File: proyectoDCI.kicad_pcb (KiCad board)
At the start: 2 copper layers, 45 x 20 mm, 27 parts, among them P1 CONN_02X04, P2 CONN_01X01, P3 GSG-RF-CONN, P4 GSG-RF-CONN, U1 AD5933, U2 ADG849, U3 AD8606, U4 ASFLMB-16.000MHZ-LY-T, U5 ADP150

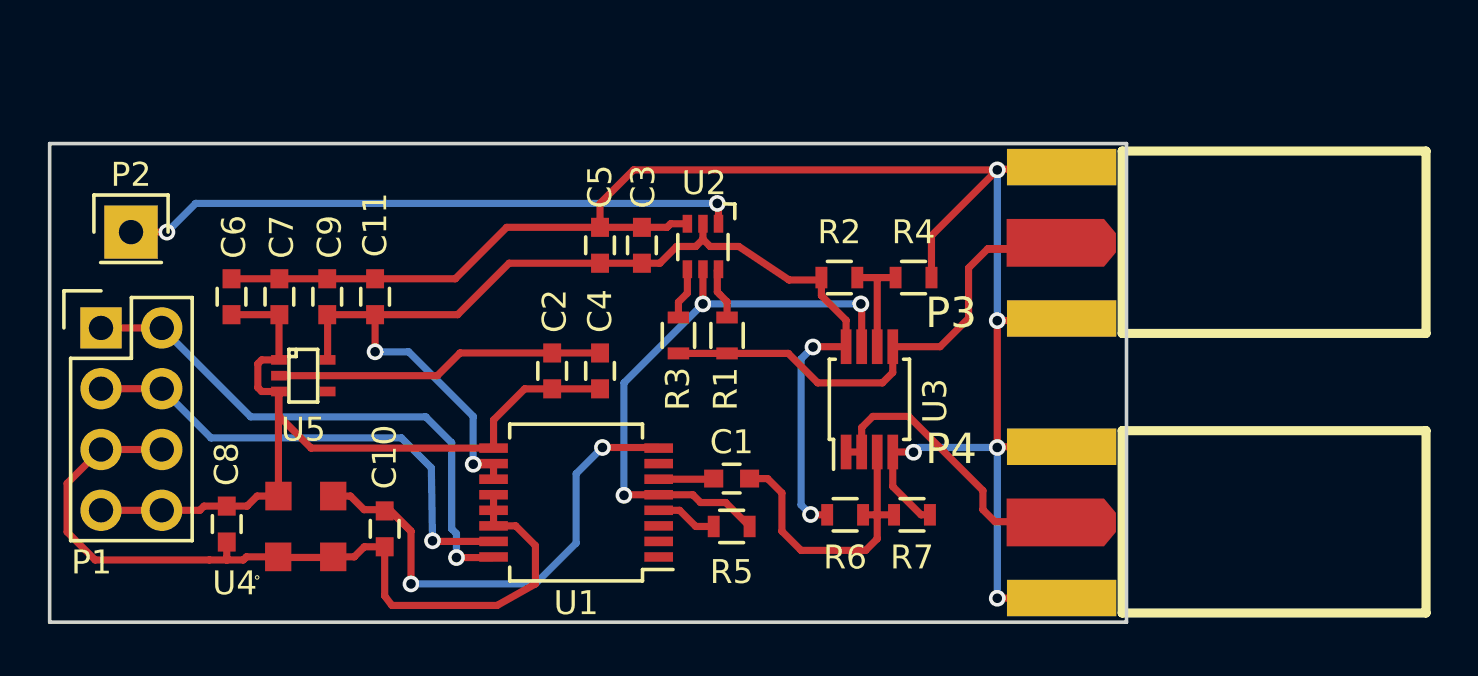
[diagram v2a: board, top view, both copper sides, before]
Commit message: Se modifico el rotulo y se agregaron aclaraciones del proceso de fabricacion
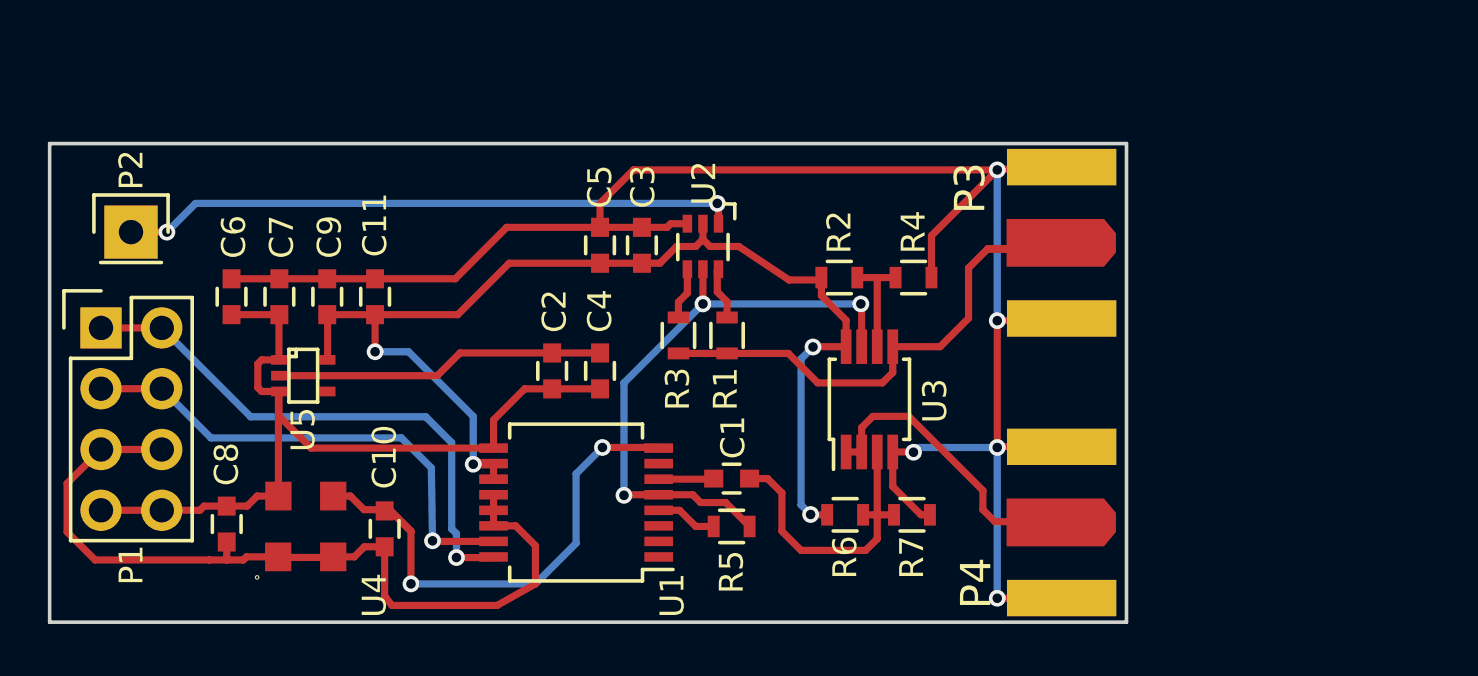
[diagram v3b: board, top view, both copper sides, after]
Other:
- board text added: "* Clearance -> 0,15 mm * Ancho de pista -> 0,15 mm * Diámetro vía -> 0,70 mm * Agujero vía -> 0,40 mm (Perfil: Mayer 6 mils ver proyectoDCI/doc/Fab)"
- board text added: "Acabado: HASL Espesor cobre: 1oz"
- board text added: "Espesor: 1,6 mm"
- board text added: "N° Capas = 2"
- board text added: "Reglas de fabricación"
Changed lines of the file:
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@@
     (area 149.924999 100.424999 195.075001 120.575001)
     (thickness 1.6)
-    (drawings 44)
+    (drawings 73)
     (tracks 241)
     (zones 0)
@@
   )
   (page A4)
+  (title_block
+    (title "PMOD Medidor de impedancia")
+    (date 2016-12-10)
+    (rev "Rev A")
+    (company CESE)
+    (comment 1 "Autor: LAROSA, F.")
+    (comment 2 "Revisor: GIGLIOTTI, E.")
+  )
   (layers
-    (0 F.Cu signal)
+    (0 F.Cu signal hide)
     (31 B.Cu signal hide)
     (32 B.Adhes user)
@@
   (module SMA_EDGE:SMA_EDGE (layer F.Cu)
     (at 201.168 115.062)
-    (fp_text reference P4 (at -13.5 -1.8) (layer F.SilkS)
+    (fp_text reference P4 (at -12.446 3.81 90) (layer F.SilkS)
       (effects (font (thickness 0.3048)))
     )
@@
       (effects (font (thickness 0.3048)))
     )
-    (fp_line (start -6.35 -2.5654) (end -6.35 5.0546) (layer F.SilkS) (width 0.381))
-    (fp_line (start -6.35 5.0546) (end 6.35 5.0546) (layer F.SilkS) (width 0.381))
-    (fp_line (start 6.35 5.0546) (end 6.35 -2.5654) (layer F.SilkS) (width 0.381))
-    (fp_line (start 6.35 -2.5654) (end -6.35 -2.5654) (layer F.SilkS) (width 0.381))
     (pad 0 connect rect (at -8.8773 -1.89484) (size 4.572 1.524) (layers *.Cu F.Mask)
       (net 2 GND))
@@
     (pad 1 connect rect (at -9.144 1.27) (size 4.07162 1.99898) (layers F.Cu F.Mask)
       (net 14 /Senal/COUT))
-    (model SMA_EDGE.wrl
+    (model /home/fsl/Documentos/ESE/Kicad/Proyecto/proyectoDCI/proyecto.3dshapes/SMAEdge.wrl
       (at (xyz -0.205 -0.05 -0.12))
-      (scale (xyz 1.3 1.3 1.3))
+      (scale (xyz 1 1 1))
       (rotate (xyz 270 0 180))
     )
@@
   (module SMA_EDGE:SMA_EDGE (layer F.Cu)
     (at 201.168 103.378)
-    (fp_text reference P3 (at -13.5 4.2) (layer F.SilkS)
+    (fp_text reference P3 (at -12.7 -1.016 90) (layer F.SilkS)
       (effects (font (thickness 0.3048)))
     )
@@
       (effects (font (thickness 0.3048)))
     )
-    (fp_line (start -6.35 -2.5654) (end -6.35 5.0546) (layer F.SilkS) (width 0.381))
-    (fp_line (start -6.35 5.0546) (end 6.35 5.0546) (layer F.SilkS) (width 0.381))
-    (fp_line (start 6.35 5.0546) (end 6.35 -2.5654) (layer F.SilkS) (width 0.381))
-    (fp_line (start 6.35 -2.5654) (end -6.35 -2.5654) (layer F.SilkS) (width 0.381))
     (pad 0 connect rect (at -8.8773 -1.89484) (size 4.572 1.524) (layers *.Cu F.Mask)
       (net 2 GND))
@@
     (pad 1 connect rect (at -9.144 1.27) (size 4.07162 1.99898) (layers F.Cu F.Mask)
       (net 15 /Senal/CIN))
-    (model SMA_EDGE.wrl
-      (at (xyz -0.205 -0.05 -0.12))
-      (scale (xyz 1.3 1.3 1.3))
-      (rotate (xyz 270 0 180))
+    (model /home/fsl/Documentos/ESE/Kicad/Proyecto/proyectoDCI/proyecto.3dshapes/SMAEdge.wrl
+      (at (xyz 0 0 0))
+      (scale (xyz 1 1 1))
+      (rotate (xyz 0 0 0))
     )
   )
   (module propios:TCXO (layer F.Cu)
     (at 160.7 116.5)
-    (fp_text reference U4 (at -2.966 2.372) (layer F.SilkS)
+    (fp_text reference U4 (at 2.876 2.88 90) (layer F.SilkS)
       (effects (font (size 1 1) (thickness 0.15)))
     )
@@
     (pad 3 smd rect (at 1.15 -1.27) (size 1.1 1.2) (layers F.Cu F.Paste F.Mask)
       (net 9 /Otros/MCLK))
+    (model Oscillators.3dshapes/TCXO_G158.wrl
+      (at (xyz 0 0 0))
+      (scale (xyz 0.15 0.3 0.3))
+      (rotate (xyz 0 0 90))
+    )
   )
   (module Capacitors_SMD:C_0603 (layer F.Cu)
@@
     (tags "capacitor 0603")
     (attr smd)
-    (fp_text reference C1 (at 0 1.524 180) (layer F.SilkS)
+    (fp_text reference C1 (at -0.062 1.724 270) (layer F.SilkS)
       (effects (font (size 1 1) (thickness 0.15)))
     )
@@
     (tags "resistor 0603")
     (attr smd)
-    (fp_text reference R2 (at 0 -1.9) (layer F.SilkS)
+    (fp_text reference R2 (at 0 -1.9 90) (layer F.SilkS)
       (effects (font (size 1 1) (thickness 0.15)))
     )
@@
     (tags "resistor 0603")
     (attr smd)
-    (fp_text reference R4 (at 0 -1.9) (layer F.SilkS)
+    (fp_text reference R4 (at 0 -1.9 90) (layer F.SilkS)
       (effects (font (size 1 1) (thickness 0.15)))
     )
@@
     (tags "resistor 0603")
     (attr smd)
-    (fp_text reference R5 (at 0 -1.9 180) (layer F.SilkS)
+    (fp_text reference R5 (at 0 -1.9 270) (layer F.SilkS)
       (effects (font (size 1 1) (thickness 0.15)))
     )
@@
     (tags "resistor 0603")
     (attr smd)
-    (fp_text reference R6 (at 0 1.778) (layer F.SilkS)
+    (fp_text reference R6 (at 0 1.778 90) (layer F.SilkS)
       (effects (font (size 1 1) (thickness 0.15)))
     )
@@
     (tags "resistor 0603")
     (attr smd)
-    (fp_text reference R7 (at 0 1.778) (layer F.SilkS)
+    (fp_text reference R7 (at 0 1.778 90) (layer F.SilkS)
       (effects (font (size 1 1) (thickness 0.15)))
     )
@@
     (tags SC-70-6)
     (attr smd)
-    (fp_text reference U2 (at -0.05 2.65 180) (layer F.SilkS)
+    (fp_text reference U2 (at -0.05 2.65 270) (layer F.SilkS)
       (effects (font (size 1 1) (thickness 0.15)))
     )
@@
     (descr "SC70-5 SOT323-5")
     (attr smd)
-    (fp_text reference U5 (at 2.25 0 360) (layer F.SilkS)
+    (fp_text reference U5 (at 2.25 0 450) (layer F.SilkS)
       (effects (font (size 1 1) (thickness 0.15)))
     )
@@
     (descr "Through hole pin header")
     (tags "pin header")
-    (fp_text reference P1 (at -0.396 9.796) (layer F.SilkS)
+    (fp_text reference P1 (at 1.27 9.906 90) (layer F.SilkS)
       (effects (font (size 1 1) (thickness 0.15)))
     )
@@
     (descr "Through hole pin header")
     (tags "pin header")
-    (fp_text reference P2 (at 0 -2.4) (layer F.SilkS)
+    (fp_text reference P2 (at 0.016 -2.6 90) (layer F.SilkS)
       (effects (font (size 1 1) (thickness 0.15)))
     )
@@
     (tags "SSOP 0.65")
     (attr smd)
-    (fp_text reference U1 (at 0 -4.2 180) (layer F.SilkS)
+    (fp_text reference U1 (at -4.022 -3.88 270) (layer F.SilkS)
       (effects (font (size 1 1) (thickness 0.15)))
     )
@@
     )
   )
+  (gr_text "N° Capas = 2" (at 203.708 130.048) (layer Dwgs.User)
+    (effects (font (size 1.5 1.5) (thickness 0.3)))
+  )
+  (gr_text "Acabado: HASL\nEspesor cobre: 1oz" (at 203.962 138.684) (layer Dwgs.User)
+    (effects (font (size 1.5 1.5) (thickness 0.3)))
+  )
+  (gr_text "Espesor: 1,6 mm" (at 203.708 133.858) (layer Dwgs.User)
+    (effects (font (size 1.2 1.2) (thickness 0.2)))
+  )
+  (gr_line (start 196.088 135.636) (end 196.088 135.128) (angle 90) (layer Dwgs.User) (width 0.2))
+  (gr_line (start 211.074 135.636) (end 196.088 135.636) (angle 90) (layer Dwgs.User) (width 0.2))
+  (gr_line (start 211.074 135.128) (end 211.074 135.636) (angle 90) (layer Dwgs.User) (width 0.2))
+  (gr_line (start 196.088 135.128) (end 211.074 135.128) (angle 90) (layer Dwgs.User) (width 0.2))
+  (gr_line (start 196.088 132.08) (end 211.074 132.08) (angle 90) (layer Dwgs.User) (width 0.2))
+  (gr_line (start 196.088 132.08) (end 196.088 132.588) (angle 90) (layer Dwgs.User) (width 0.2))
+  (gr_line (start 196.088 132.588) (end 211.074 132.588) (angle 90) (layer Dwgs.User) (width 0.2))
+  (gr_line (start 211.074 132.588) (end 211.074 132.334) (angle 90) (layer Dwgs.User) (width 0.2))
+  (gr_line (start 211.074 132.334) (end 211.074 132.08) (angle 90) (layer Dwgs.User) (width 0.2))
+  (gr_line (start 211.074 132.334) (end 211.074 132.08) (angle 90) (layer Dwgs.User) (width 0.2))
+  (gr_line (start 211.074 132.588) (end 211.074 132.334) (angle 90) (layer Dwgs.User) (width 0.2))
+  (gr_line (start 196.088 132.588) (end 211.074 132.588) (angle 90) (layer Dwgs.User) (width 0.2))
+  (gr_line (start 196.088 132.08) (end 196.088 132.588) (angle 90) (layer Dwgs.User) (width 0.2))
+  (gr_line (start 196.088 132.08) (end 211.074 132.08) (angle 90) (layer Dwgs.User) (width 0.2))
+  (gr_line (start 196.088 132.08) (end 211.074 132.08) (angle 90) (layer Dwgs.User) (width 0.2))
+  (gr_line (start 196.088 132.08) (end 196.088 132.588) (angle 90) (layer Dwgs.User) (width 0.2))
+  (gr_line (start 196.088 132.588) (end 211.074 132.588) (angle 90) (layer Dwgs.User) (width 0.2))
+  (gr_line (start 211.074 132.588) (end 211.074 132.334) (angle 90) (layer Dwgs.User) (width 0.2))
+  (gr_line (start 211.074 132.334) (end 211.074 132.08) (angle 90) (layer Dwgs.User) (width 0.2))
+  (gr_line (start 211.074 132.334) (end 211.074 132.08) (angle 90) (layer Dwgs.User) (width 0.2))
+  (gr_line (start 211.074 132.588) (end 211.074 132.334) (angle 90) (layer Dwgs.User) (width 0.2))
+  (gr_line (start 196.088 132.588) (end 211.074 132.588) (angle 90) (layer Dwgs.User) (width 0.2))
+  (gr_line (start 196.088 132.08) (end 196.088 132.588) (angle 90) (layer Dwgs.User) (width 0.2))
+  (gr_line (start 196.088 132.08) (end 211.074 132.08) (angle 90) (layer Dwgs.User) (width 0.2))
+  (gr_text "* Clearance  -> 0,15 mm\n* Ancho de pista -> 0,15 mm\n* Diámetro vía -> 0,70 mm\n* Agujero vía -> 0,40 mm\n(Perfil: Mayer 6 mils ver proyectoDCI/doc/Fab)" (at 135.89 138.43) (layer Dwgs.User)
+    (effects (font (size 1.5 1.5) (thickness 0.3)) (justify left))
+  )
+  (gr_text "Reglas de fabricación" (at 148.59 130.302) (layer Dwgs.User)
+    (effects (font (size 1.5 1.5) (thickness 0.3)))
+  )
   (dimension 45 (width 0.3) (layer Dwgs.User)

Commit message: Se agrego leyenda del proyecto y vias adicionales para unir los planos de tierra
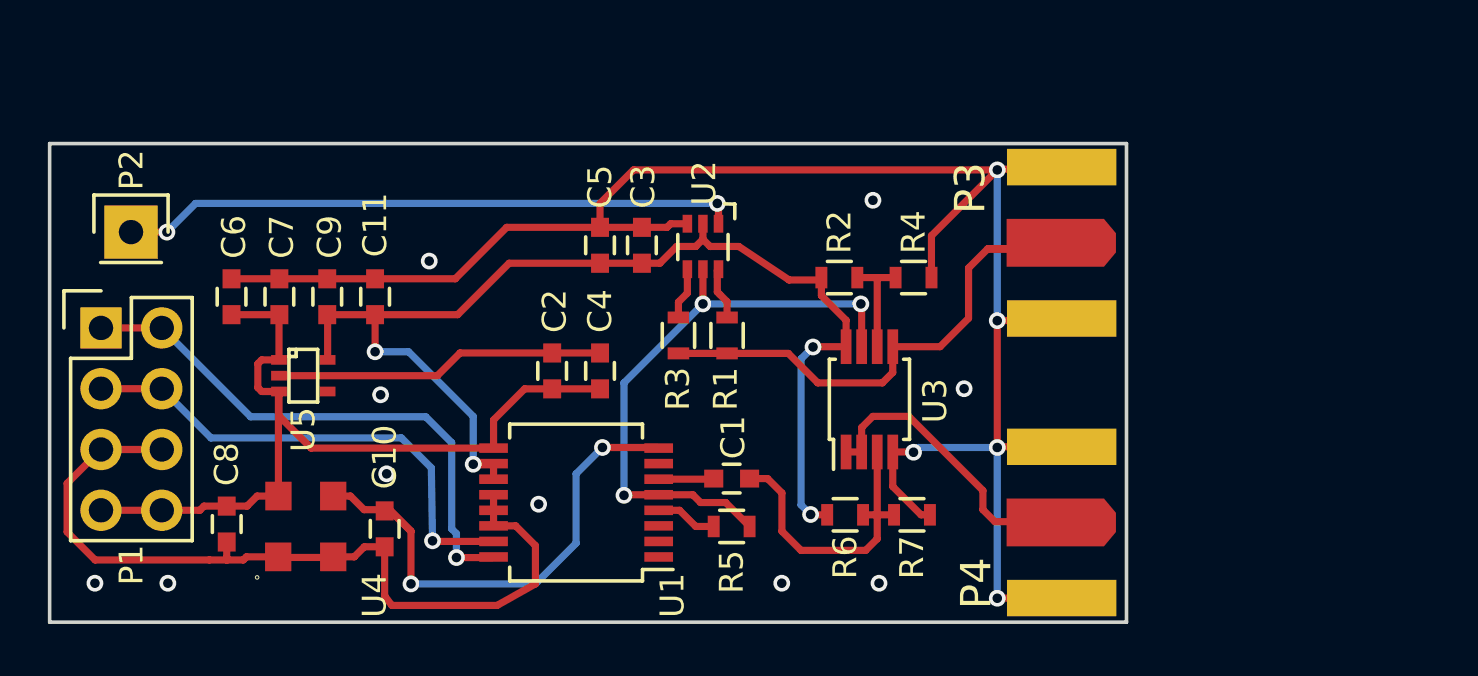
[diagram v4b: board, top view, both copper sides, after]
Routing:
- net GND: vias 5 -> 15
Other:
- board text added: "Medidor de impedancia v1.0"
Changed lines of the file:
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@@
     (area 149.924999 100.424999 195.075001 120.575001)
     (thickness 1.6)
-    (drawings 73)
-    (tracks 241)
+    (drawings 74)
+    (tracks 251)
     (zones 0)
     (modules 27)
@@
   )
   (layers
-    (0 F.Cu signal hide)
-    (31 B.Cu signal hide)
+    (0 F.Cu signal)
+    (31 B.Cu signal)
     (32 B.Adhes user)
     (33 F.Adhes user)
@@
     )
   )
+  (gr_text "Medidor de impedancia v1.0" (at 171.958 118.872) (layer B.SilkS)
+    (effects (font (size 1.5 1.5) (thickness 0.3)) (justify mirror))
+  )
   (gr_text "N° Capas = 2" (at 203.708 130.048) (layer Dwgs.User)
     (effects (font (size 1.5 1.5) (thickness 0.3)))
@@
   (segment (start 157.6 107.65) (end 159.6 107.65) (width 0.3) (layer F.Cu) (net 1))
   (segment (start 171 110.75) (end 173 110.75) (width 0.3) (layer F.Cu) (net 1))
+  (via (at 184.404 102.87) (size 0.7) (drill 0.4) (layers F.Cu B.Cu) (net 2))
+  (via (at 188.214 110.744) (size 0.7) (drill 0.4) (layers F.Cu B.Cu) (net 2))
+  (via (at 184.658 118.872) (size 0.7) (drill 0.4) (layers F.Cu B.Cu) (net 2))
+  (via (at 180.594 118.872) (size 0.7) (drill 0.4) (layers F.Cu B.Cu) (net 2))
+  (via (at 170.434 115.57) (size 0.7) (drill 0.4) (layers F.Cu B.Cu) (net 2))
+  (via (at 163.83 110.998) (size 0.7) (drill 0.4) (layers F.Cu B.Cu) (net 2))
+  (via (at 165.862 105.41) (size 0.7) (drill 0.4) (layers F.Cu B.Cu) (net 2))
+  (via (at 164.084 114.3) (size 0.7) (drill 0.4) (layers F.Cu B.Cu) (net 2))
+  (via (at 154.94 118.872) (size 0.7) (drill 0.4) (layers F.Cu B.Cu) (net 2))
+  (via (at 151.892 118.872) (size 0.7) (drill 0.4) (layers F.Cu B.Cu) (net 2))
   (segment (start 161.85 117.77) (end 162.73 117.77) (width 0.3) (layer F.Cu) (net 2))
   (segment (start 163.15 117.35) (end 164 117.35) (width 0.3) (layer F.Cu) (net 2))

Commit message: Corregido error de tipeo en REQUERIMIENTOS DEL PROYECTO
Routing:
- net GND: vias 15 -> 5
- net (no net): vias 0 -> 10
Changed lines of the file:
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@@
     (links 71)
     (no_connects 0)
-    (area 149.924999 100.424999 195.075001 120.575001)
+    (area 131.350001 99.684 215.156001 144.88)
     (thickness 1.6)
     (drawings 74)
@@
   (layers
     (0 F.Cu signal)
-    (31 B.Cu signal)
+    (31 B.Cu signal hide)
     (32 B.Adhes user)
     (33 F.Adhes user)
@@
     (pad 1 connect rect (at -9.144 1.27) (size 4.07162 1.99898) (layers F.Cu F.Mask)
       (net 14 /Senal/COUT))
-    (model /home/fsl/Documentos/ESE/Kicad/Proyecto/proyectoDCI/proyecto.3dshapes/SMAEdge.wrl
+    (model ${KIPRJMOD}/proyecto.3dshapes/SMAEdge.wrl
       (at (xyz -0.205 -0.05 -0.12))
       (scale (xyz 1 1 1))
@@
     (pad 1 connect rect (at -9.144 1.27) (size 4.07162 1.99898) (layers F.Cu F.Mask)
       (net 15 /Senal/CIN))
-    (model /home/fsl/Documentos/ESE/Kicad/Proyecto/proyectoDCI/proyecto.3dshapes/SMAEdge.wrl
+    (model ${KIPRJMOD}/proyectoDCI/proyecto.3dshapes/SMAEdge.wrl
       (at (xyz 0 0 0))
       (scale (xyz 1 1 1))
@@
   (gr_line (start 195.056 110.73) (end 215.056 110.73) (angle 90) (layer Dwgs.User) (width 0.2))
   (gr_line (start 150 113) (end 141 113) (angle 90) (layer Dwgs.User) (width 0.2))
+  (via (at 184.404 102.87) (size 0.7) (drill 0.4) (layers F.Cu B.Cu) (net 0))
+  (via (at 188.214 110.744) (size 0.7) (drill 0.4) (layers F.Cu B.Cu) (net 0))
+  (via (at 184.658 118.872) (size 0.7) (drill 0.4) (layers F.Cu B.Cu) (net 0))
+  (via (at 180.594 118.872) (size 0.7) (drill 0.4) (layers F.Cu B.Cu) (net 0))
+  (via (at 170.434 115.57) (size 0.7) (drill 0.4) (layers F.Cu B.Cu) (net 0))
+  (via (at 163.83 110.998) (size 0.7) (drill 0.4) (layers F.Cu B.Cu) (net 0))
+  (via (at 165.862 105.41) (size 0.7) (drill 0.4) (layers F.Cu B.Cu) (net 0))
+  (via (at 164.084 114.3) (size 0.7) (drill 0.4) (layers F.Cu B.Cu) (net 0))
+  (via (at 154.94 118.872) (size 0.7) (drill 0.4) (layers F.Cu B.Cu) (net 0))
+  (via (at 151.892 118.872) (size 0.7) (drill 0.4) (layers F.Cu B.Cu) (net 0))
   (segment (start 154.686 115.824) (end 156.276 115.824) (width 0.3) (layer F.Cu) (net 1))
   (segment (start 156.45 115.65) (end 157.4 115.65) (width 0.3) (layer F.Cu) (net 1))
@@
   (segment (start 157.6 107.65) (end 159.6 107.65) (width 0.3) (layer F.Cu) (net 1))
   (segment (start 171 110.75) (end 173 110.75) (width 0.3) (layer F.Cu) (net 1))
-  (via (at 184.404 102.87) (size 0.7) (drill 0.4) (layers F.Cu B.Cu) (net 2))
-  (via (at 188.214 110.744) (size 0.7) (drill 0.4) (layers F.Cu B.Cu) (net 2))
-  (via (at 184.658 118.872) (size 0.7) (drill 0.4) (layers F.Cu B.Cu) (net 2))
-  (via (at 180.594 118.872) (size 0.7) (drill 0.4) (layers F.Cu B.Cu) (net 2))
-  (via (at 170.434 115.57) (size 0.7) (drill 0.4) (layers F.Cu B.Cu) (net 2))
-  (via (at 163.83 110.998) (size 0.7) (drill 0.4) (layers F.Cu B.Cu) (net 2))
-  (via (at 165.862 105.41) (size 0.7) (drill 0.4) (layers F.Cu B.Cu) (net 2))
-  (via (at 164.084 114.3) (size 0.7) (drill 0.4) (layers F.Cu B.Cu) (net 2))
-  (via (at 154.94 118.872) (size 0.7) (drill 0.4) (layers F.Cu B.Cu) (net 2))
-  (via (at 151.892 118.872) (size 0.7) (drill 0.4) (layers F.Cu B.Cu) (net 2))
   (segment (start 161.85 117.77) (end 162.73 117.77) (width 0.3) (layer F.Cu) (net 2))
   (segment (start 163.15 117.35) (end 164 117.35) (width 0.3) (layer F.Cu) (net 2))
